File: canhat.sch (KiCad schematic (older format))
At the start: 42 parts, among them J1 Raspberry_Pi_2_3, J2 CAN In/Out/GND, J3 GPIO, J5 12V, U1 MCP2515-xSO, U2 SN65HVD234, U3 AT24C32-SSHM, U4 AP63205, Y1 16MHz

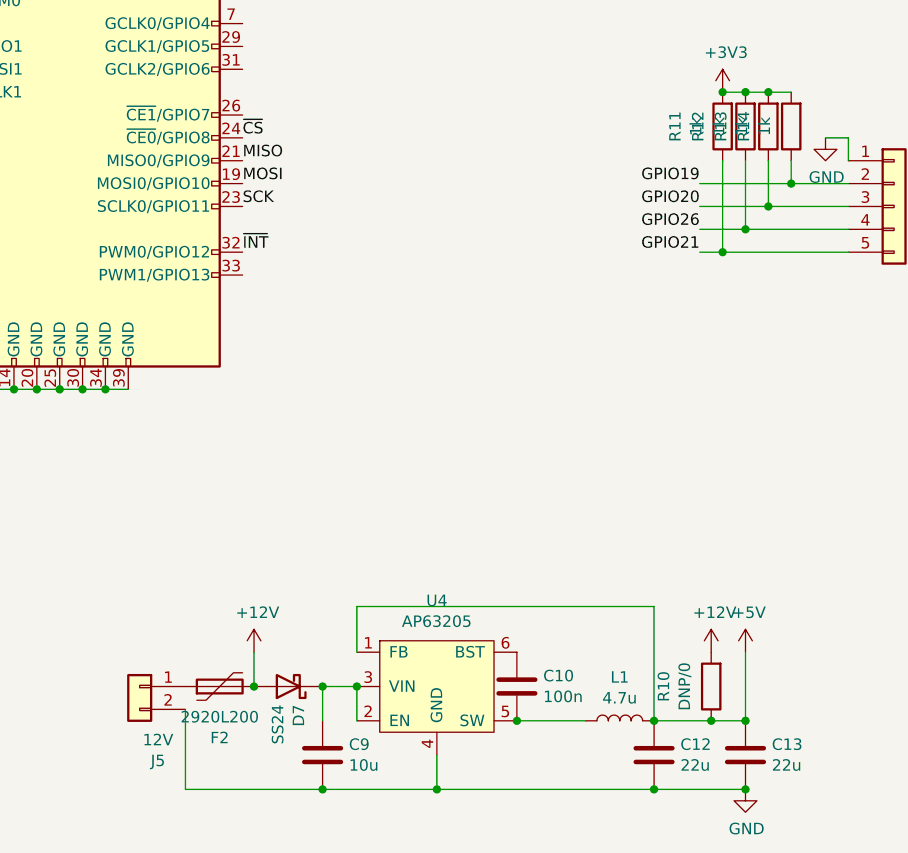
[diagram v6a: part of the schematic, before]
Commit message: Reordered parts an added GPIO pins
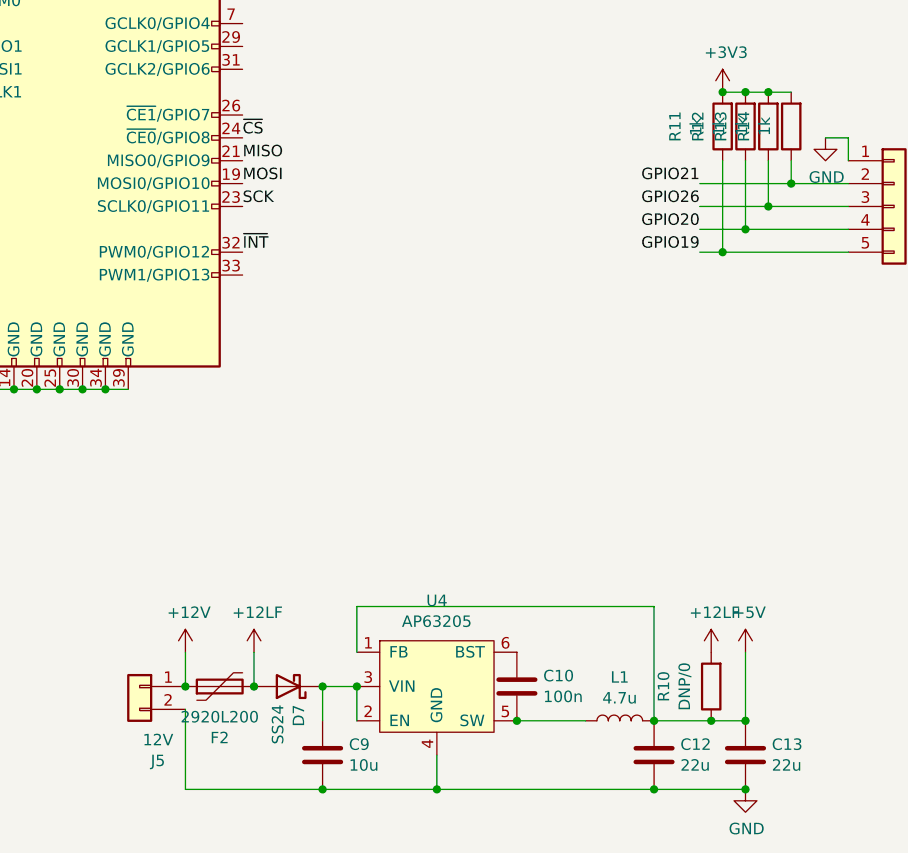
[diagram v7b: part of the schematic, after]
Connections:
- net +12V: now also F2.1, J5.1 (Pin_1); no longer D7.2 (A), F2.2, R10.2
- net GPIO19: now also J3.5 (Pin_5), R11.1; no longer J3.2 (Pin_2), R14.1
- net GPIO20: now also J3.4 (Pin_4), R12.1; no longer J3.3 (Pin_3), R13.1
- net GPIO21: now also J3.2 (Pin_2), R14.1; no longer J3.5 (Pin_5), R11.1
- net GPIO26: now also J3.3 (Pin_3), R13.1; no longer J3.4 (Pin_4), R12.1
- new net +12LF: D7.2 (A), F2.2, R10.2
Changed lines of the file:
@@
 L power:+12V #PWR07
 U 1 1 5DC9A6CE
-P 2900 6550
-F 0 "#PWR07" H 2900 6400 50  0001 C CNN
-F 1 "+12V" H 2915 6723 50  0000 C CNN
-F 2 "" H 2900 6550 50  0001 C CNN
-F 3 "" H 2900 6550 50  0001 C CNN
-	1    2900 6550
+P 2600 6550
+F 0 "#PWR07" H 2600 6400 50  0001 C CNN
+F 1 "+12V" H 2615 6723 50  0000 C CNN
+F 2 "" H 2600 6550 50  0001 C CNN
+F 3 "" H 2600 6550 50  0001 C CNN
+	1    2600 6550
 	1    0    0    -1
 $EndComp
@@
 F 3 "" H 5050 6550 50  0001 C CNN
 	1    5050 6550
-	1    0    0    -1
-$EndComp
-$Comp
-L power:+12V #PWR0114
-U 1 1 5DCDFA49
-P 4900 6550
-F 0 "#PWR0114" H 4900 6400 50  0001 C CNN
-F 1 "+12V" H 4915 6723 50  0000 C CNN
-F 2 "" H 4900 6550 50  0001 C CNN
-F 3 "" H 4900 6550 50  0001 C CNN
-	1    4900 6550
 	1    0    0    -1
 $EndComp
@@
 Text Label 1250 4100 2    50   ~ 0
 GPIO21
+Text Label 4850 4800 2    50   ~ 0
+GPIO19
+Text Label 4850 4600 2    50   ~ 0
+GPIO26
+Text Label 4850 4700 2    50   ~ 0
+GPIO20
 Text Label 4850 4500 2    50   ~ 0
-GPIO19
-Text Label 4850 4700 2    50   ~ 0
-GPIO26
-Text Label 4850 4600 2    50   ~ 0
-GPIO20
-Text Label 4850 4800 2    50   ~ 0
 GPIO21
 $Comp
@@
 Wire Wire Line
 	3350 6350 4650 6350
+$Comp
+L power:+12LF #PWR0114
+U 1 1 5F0C1AE1
+P 2900 6550
+F 0 "#PWR0114" H 2900 6400 50  0001 C CNN
+F 1 "+12LF" H 2915 6723 50  0000 C CNN
+F 2 "" H 2900 6550 50  0001 C CNN
+F 3 "" H 2900 6550 50  0001 C CNN
+	1    2900 6550
+	1    0    0    -1
+$EndComp
+Wire Wire Line
+	2600 6550 2600 6700
+Connection ~ 2600 6700
+$Comp
+L power:+12LF #PWR0122
+U 1 1 5F0C4323
+P 4900 6550
+F 0 "#PWR0122" H 4900 6400 50  0001 C CNN
+F 1 "+12LF" H 4915 6723 50  0000 C CNN
+F 2 "" H 4900 6550 50  0001 C CNN
+F 3 "" H 4900 6550 50  0001 C CNN
+	1    4900 6550
+	1    0    0    -1
+$EndComp
 $EndSCHEMATC
